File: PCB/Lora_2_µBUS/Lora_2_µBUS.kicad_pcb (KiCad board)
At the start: 2 copper layers, 25.4 x 29.2 mm, 2 parts

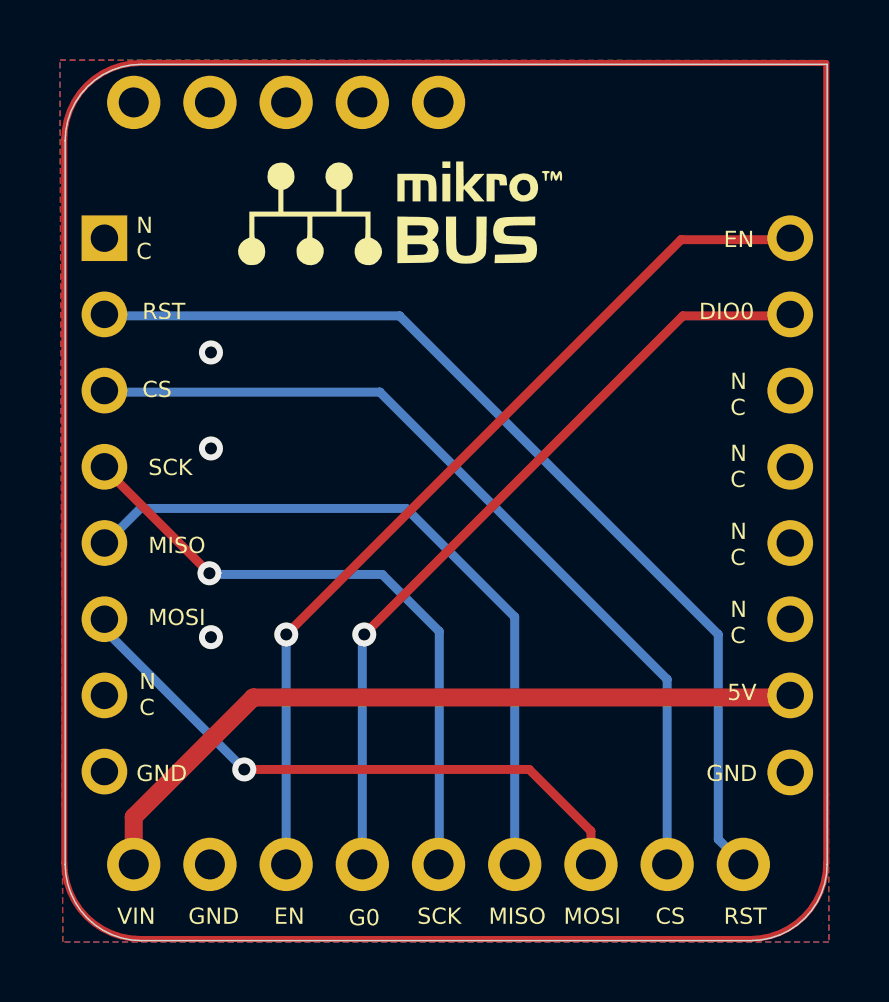
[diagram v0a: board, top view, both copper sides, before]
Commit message: Updated µBus adapter
power redirected to 3.3V
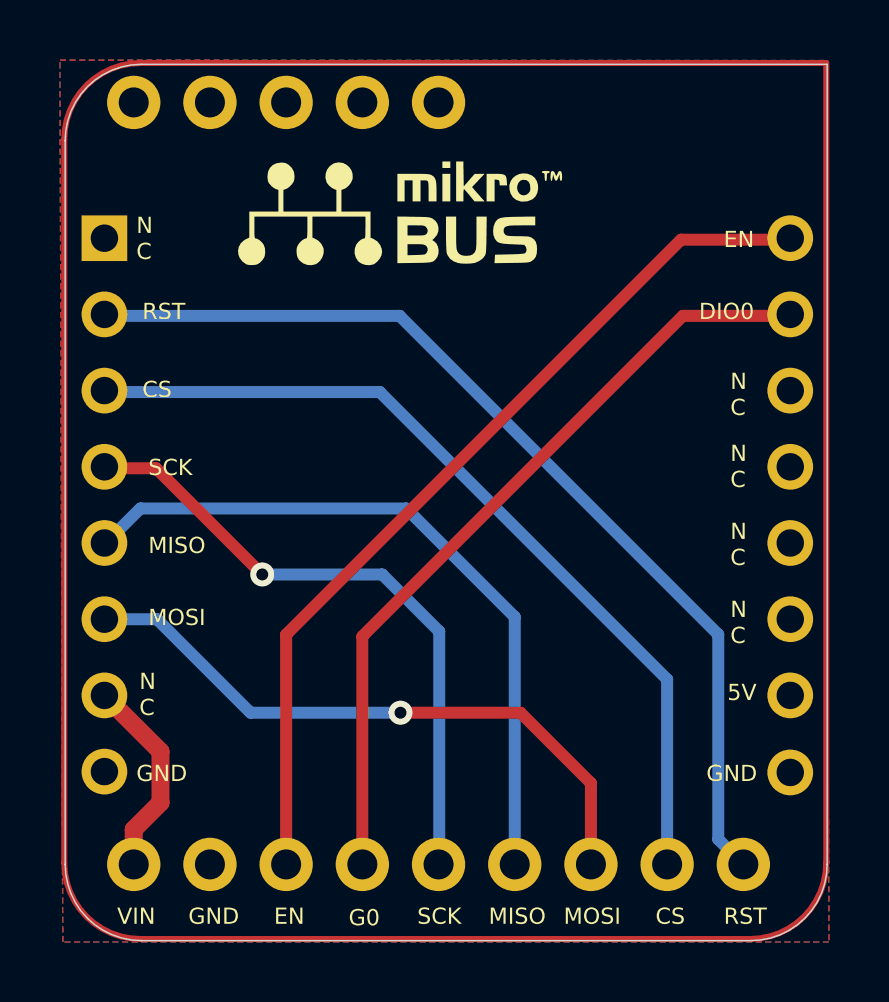
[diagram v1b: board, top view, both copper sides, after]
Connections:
- LoRA_breakout1 pad 6: /5V -> /3.3
- MikroBUS_adapter1 pad 15: /5V -> unconnected-(MikroBUS_adapter1-5V-Pad15)
- MikroBUS_adapter1 pad 7: unconnected-(MikroBUS_adapter1-3.3V-Pad7) -> /3.3
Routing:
- net /5V: track 25.1 -> 0.00 mm
- net /3.3: track 0.00 -> 6.78 mm
- net /MOSI: track 20.4 -> 21.8 mm
- net /DIO_1: vias 1 -> 0
- net /DIO_0: vias 1 -> 0
- net /GND: vias 3 -> 0
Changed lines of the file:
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@@
 	(net 9 "/MOSI")
 	(net 10 "/MISO")
-	(net 11 "/5V")
+	(net 11 "/3.3")
 	(net 12 "/DIO_0")
 	(net 13 "unconnected-(LoRA_breakout1-G2-Pad2)")
 	(net 14 "/CS")
-	(net 15 "unconnected-(MikroBUS_adapter1-3.3V-Pad7)")
+	(net 15 "unconnected-(MikroBUS_adapter1-5V-Pad15)")
 	(net 16 "unconnected-(MikroBUS_adapter1-Rx-Pad11)")
 	(net 17 "unconnected-(MikroBUS_adapter1-AN-Pad1)")
@@
 			(layers "*.Cu" "*.Mask")
 			(remove_unused_layers no)
-			(net 11 "/5V")
+			(net 11 "/3.3")
 			(pinfunction "Vin")
 			(pintype "power_in")
@@
 			(layers "*.Cu" "*.Mask")
 			(remove_unused_layers no)
-			(net 15 "unconnected-(MikroBUS_adapter1-3.3V-Pad7)")
+			(net 11 "/3.3")
 			(pinfunction "3.3V")
 			(pintype "input")
@@
 			(layers "*.Cu" "*.Mask")
 			(remove_unused_layers no)
-			(net 11 "/5V")
+			(net 15 "unconnected-(MikroBUS_adapter1-5V-Pad15)")
 			(pinfunction "5V")
 			(pintype "input")
@@
 	)
 	(segment
+		(start 140.992 88.772)
+		(end 137.412 88.772)
+		(width 0.4)
+		(layer "F.Cu")
+		(net 4)
+	)
+	(segment
 		(start 137.412 88.772)
-		(end 140.992 88.772)
-		(width 0.3)
+		(end 126.728 99.456)
+		(width 0.4)
 		(layer "F.Cu")
 		(net 4)
 	)
 	(segment
-		(start 126.792 99.392)
-		(end 137.412 88.772)
-		(width 0.3)
-		(layer "F.Cu")
-		(net 4)
-	)
-	(via
-		(at 126.792 99.392)
-		(size 0.8)
-		(drill 0.4)
-		(layers "F.Cu" "B.Cu")
-		(net 4)
-	)
-	(segment
-		(start 126.792 99.392)
-		(end 126.728 99.456)
-		(width 0.2)
-		(layer "B.Cu")
-		(net 4)
-	)
-	(segment
 		(start 126.728 99.456)
-		(end 126.728 107.062)
-		(width 0.3)
-		(layer "B.Cu")
+		(end 126.728 107.057)
+		(width 0.4)
+		(layer "F.Cu")
 		(net 4)
 	)
@@
 		(start 138.592 99.392)
 		(end 138.592 106.221)
-		(width 0.3)
+		(width 0.4)
 		(layer "B.Cu")
 		(net 6)
@@
 		(start 138.592 106.221)
 		(end 139.428 107.057)
-		(width 0.3)
+		(width 0.4)
 		(layer "B.Cu")
 		(net 6)
@@
 		(start 118.1308 88.772)
 		(end 127.972 88.772)
-		(width 0.3)
+		(width 0.4)
 		(layer "B.Cu")
 		(net 6)
@@
 		(start 127.972 88.772)
 		(end 138.592 99.392)
-		(width 0.3)
+		(width 0.4)
 		(layer "B.Cu")
 		(net 6)
 	)
 	(segment
-		(start 121.6314 97.3526)
+		(start 119.852 93.852)
 		(end 118.1308 93.852)
-		(width 0.3)
+		(width 0.4)
 		(layer "F.Cu")
 		(net 7)
 	)
+	(segment
+		(start 123.392 97.392)
+		(end 119.852 93.852)
+		(width 0.4)
+		(layer "F.Cu")
+		(net 7)
+	)
 	(via
-		(at 121.6314 97.3526)
+		(at 123.392 97.392)
 		(size 0.8)
 		(drill 0.4)
@@
 	)
 	(segment
-		(start 121.6314 97.3526)
-		(end 121.6708 97.392)
-		(width 0.2)
-		(layer "B.Cu")
-		(net 7)
-	)
-	(segment
 		(start 127.392 97.392)
 		(end 129.292 99.292)
-		(width 0.3)
+		(width 0.4)
+		(layer "B.Cu")
+		(net 7)
+	)
+	(segment
+		(start 129.292 99.292)
+		(end 129.292 107.033)
+		(width 0.4)
 		(layer "B.Cu")
 		(net 7)
@@
 	)
 	(segment
-		(start 129.292 99.292)
-		(end 129.292 107.033)
-		(width 0.3)
+		(start 123.392 97.392)
+		(end 127.392 97.392)
+		(width 0.4)
 		(layer "B.Cu")
 		(net 7)
 	)
 	(segment
-		(start 121.6708 97.392)
-		(end 127.392 97.392)
-		(width 0.3)
-		(layer "B.Cu")
-		(net 7)
+		(start 128 102)
+		(end 132 102)
+		(width 0.4)
+		(layer "F.Cu")
+		(net 9)
+	)
+	(segment
+		(start 132 102)
+		(end 134.348 104.348)
+		(width 0.4)
+		(layer "F.Cu")
+		(net 9)
+	)
+	(segment
+		(start 134.348 104.348)
+		(end 134.348 107.057)
+		(width 0.4)
+		(layer "F.Cu")
+		(net 9)
 	)
 	(via
-		(at 121.682 89.992)
-		(size 0.8)
-		(drill 0.4)
-		(layers "F.Cu" "B.Cu")
-		(free yes)
-		(net 8)
-	)
-	(via
-		(at 121.682 93.192)
-		(size 0.8)
-		(drill 0.4)
-		(layers "F.Cu" "B.Cu")
-		(free yes)
-		(net 8)
-	)
-	(via
-		(at 121.682 99.482)
-		(size 0.8)
-		(drill 0.4)
-		(layers "F.Cu" "B.Cu")
-		(free yes)
-		(net 8)
-	)
-	(segment
-		(start 132.292 103.892)
-		(end 134.348 105.948)
-		(width 0.3)
-		(layer "F.Cu")
-		(net 9)
-	)
-	(segment
-		(start 122.792 103.892)
-		(end 132.292 103.892)
-		(width 0.3)
-		(layer "F.Cu")
-		(net 9)
-	)
-	(segment
-		(start 134.348 105.948)
-		(end 134.348 107.057)
-		(width 0.3)
-		(layer "F.Cu")
-		(net 9)
-	)
-	(via
-		(at 122.792 103.892)
+		(at 128 102)
 		(size 0.8)
 		(drill 0.4)
@@
 	)
 	(segment
-		(start 122.792 103.892)
+		(start 119.8832 98.8832)
+		(end 118.1308 98.8832)
+		(width 0.4)
+		(layer "B.Cu")
+		(net 9)
+	)
+	(segment
+		(start 128 102)
+		(end 123 102)
+		(width 0.4)
+		(layer "B.Cu")
+		(net 9)
+	)
+	(segment
+		(start 123 102)
+		(end 119.8832 98.8832)
+		(width 0.4)
+		(layer "B.Cu")
+		(net 9)
+	)
+	(segment
+		(start 118.1308 98.8832)
 		(end 118.1308 99.2308)
 		(width 0.3)
@@
 		(start 131.808 107.057)
 		(end 131.808 98.808)
-		(width 0.3)
+		(width 0.4)
 		(layer "B.Cu")
 		(net 10)
@@
 		(start 128.192 95.192)
 		(end 119.3308 95.192)
-		(width 0.3)
+		(width 0.4)
 		(layer "B.Cu")
 		(net 10)
@@
 		(start 119.3308 95.192)
 		(end 118.1308 96.392)
-		(width 0.3)
+		(width 0.4)
 		(layer "B.Cu")
 		(net 10)
@@
 		(start 131.808 98.808)
 		(end 128.192 95.192)
-		(width 0.3)
+		(width 0.4)
 		(layer "B.Cu")
 		(net 10)
+	)
+	(segment
+		(start 120 105)
+		(end 120 103.2924)
+		(width 0.6)
+		(layer "F.Cu")
+		(net 11)
+	)
+	(segment
+		(start 119.108 105.892)
+		(end 120 105)
+		(width 0.6)
+		(layer "F.Cu")
+		(net 11)
+	)
+	(segment
+		(start 120 103.2924)
+		(end 118.1308 101.4232)
+		(width 0.6)
+		(layer "F.Cu")
+		(net 11)
+	)
+	(segment
+		(start 119.108 107.062)
+		(end 119.108 105.892)
+		(width 0.6)
+		(layer "F.Cu")
+		(net 11)
+	)
+	(segment
+		(start 137.352 86.232)
+		(end 124.188 99.396)
+		(width 0.4)
+		(layer "F.Cu")
+		(net 12)
+	)
+	(segment
+		(start 124.188 99.396)
+		(end 124.188 107.057)
+		(width 0.4)
+		(layer "F.Cu")
+		(net 12)
+	)
+	(segment
+		(start 140.992 86.232)
+		(end 137.352 86.232)
+		(width 0.4)
+		(layer "F.Cu")
+		(net 12)
+	)
+	(segment
+		(start 136.888 107.057)
+		(end 136.888 100.888)
+		(width 0.4)
+		(layer "B.Cu")
+		(net 14)
+	)
+	(segment
+		(start 127.312 91.312)
+		(end 118.1308 91.312)
+		(width 0.4)
+		(layer "B.Cu")
+		(net 14)
+	)
+	(segment
+		(start 136.888 100.888)
+		(end 127.312 91.312)
+		(width 0.4)
+		(layer "B.Cu")
+		(net 14)
 	)
 	(segment
@@
 		(width 0.5)
 		(layer "F.Cu")
-		(net 11)
-	)
-	(segment
-		(start 123.092 101.492)
-		(end 119.108 105.476)
-		(width 0.6)
-		(layer "F.Cu")
-		(net 11)
-	)
-	(segment
-		(start 119.108 105.476)
-		(end 119.108 107.062)
-		(width 0.6)
-		(layer "F.Cu")
-		(net 11)
-	)
-	(segment
-		(start 140.972 101.492)
-		(end 123.092 101.492)
-		(width 0.6)
-		(layer "F.Cu")
-		(net 11)
-	)
-	(segment
-		(start 124.192 99.392)
-		(end 137.352 86.232)
-		(width 0.3)
-		(layer "F.Cu")
-		(net 12)
-	)
-	(segment
-		(start 137.352 86.232)
-		(end 140.992 86.232)
-		(width 0.3)
-		(layer "F.Cu")
-		(net 12)
-	)
-	(via
-		(at 124.192 99.392)
-		(size 0.8)
-		(drill 0.4)
-		(layers "F.Cu" "B.Cu")
-		(net 12)
-	)
-	(segment
-		(start 124.192 99.392)
-		(end 124.188 99.396)
-		(width 0.3)
-		(layer "B.Cu")
-		(net 12)
-	)
-	(segment
-		(start 124.188 99.396)
-		(end 124.188 107.062)
-		(width 0.3)
-		(layer "B.Cu")
-		(net 12)
-	)
-	(segment
-		(start 136.888 107.057)
-		(end 136.888 100.888)
-		(width 0.3)
-		(layer "B.Cu")
-		(net 14)
-	)
-	(segment
-		(start 127.312 91.312)
-		(end 118.1308 91.312)
-		(width 0.3)
-		(layer "B.Cu")
-		(net 14)
-	)
-	(segment
-		(start 136.888 100.888)
-		(end 127.312 91.312)
-		(width 0.3)
-		(layer "B.Cu")
-		(net 14)
+		(net 15)
 	)
 	(zone
@@
 		(priority 1)
 		(connect_pads yes
-			(clearance 0.2)
-		)
-		(min_thickness 0.2)
+			(clearance 0.27)
+		)
+		(min_thickness 0.3)
 		(filled_areas_thickness no)
 		(fill yes
